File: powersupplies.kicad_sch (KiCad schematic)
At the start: 25 parts, among them U1 OB2222M, U2 STK17-3.3

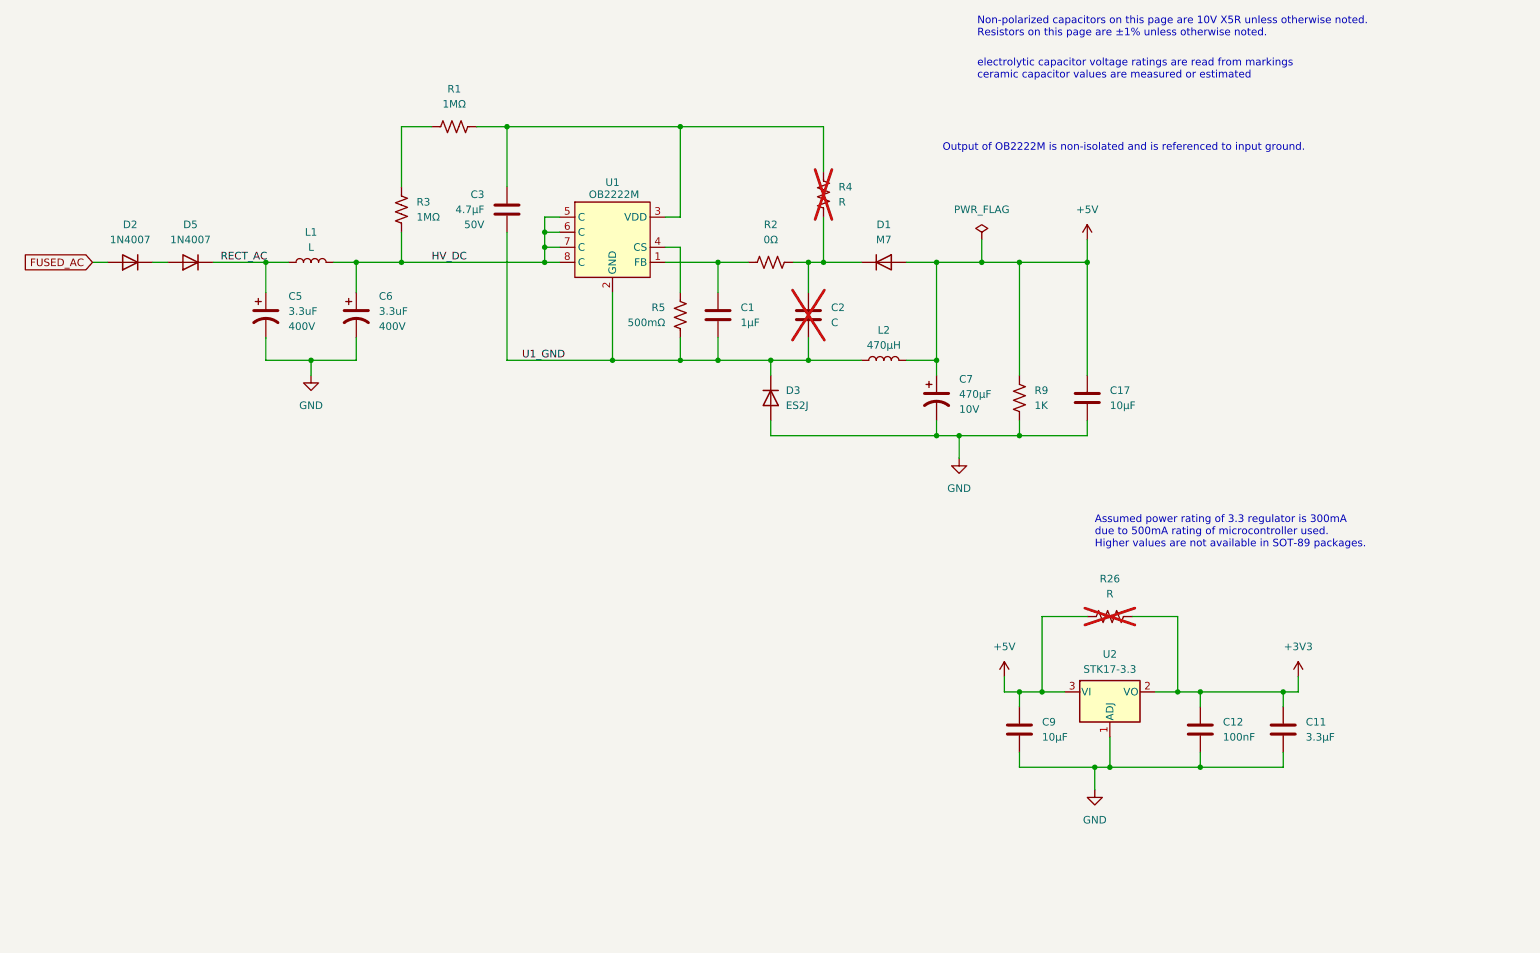
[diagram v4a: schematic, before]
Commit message: All values determined for schematic. From measurements, datasheets, or reading markings.
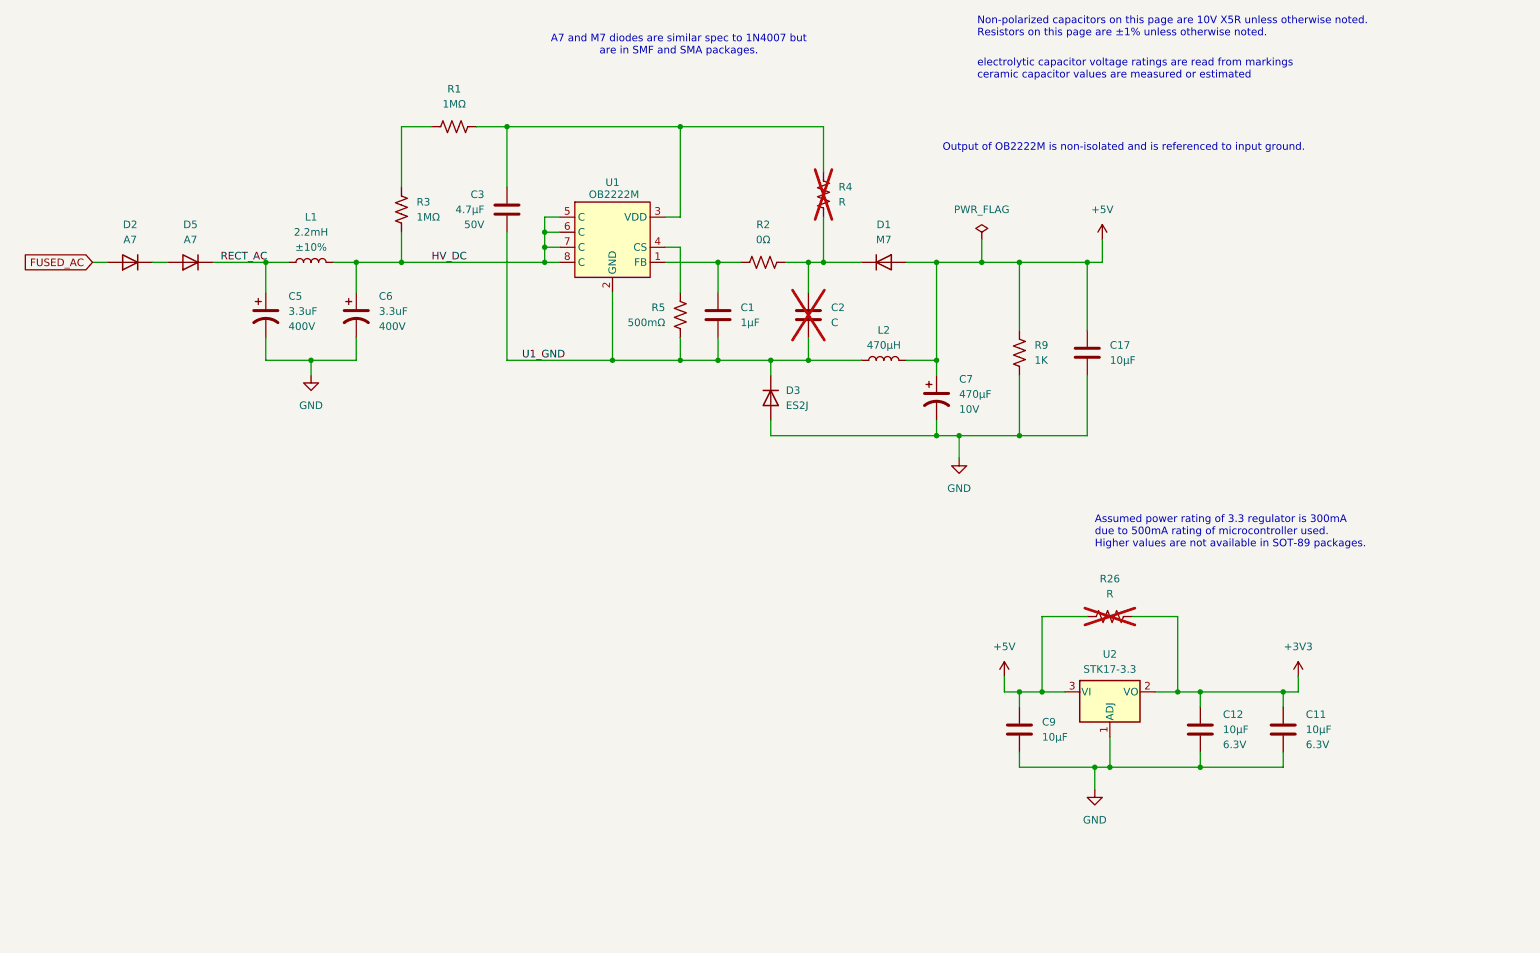
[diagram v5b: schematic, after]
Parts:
- C11: value 3.3µF -> 10µF; Voltage (none) -> 6.3V
- C12: value 100nF -> 10µF; Voltage (none) -> 6.3V
- D2, D5: value 1N4007 -> A7
- L1: value L -> 2.2mH; Tolerance (none) -> ±10%
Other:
- note added: "A7 and M7 diodes are similar spec to 1N4007 but are in SMF and SMA packages."
- moved on the sheet: C17, R2, R9
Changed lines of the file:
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@@
 		)
 	)
+	(text "A7 and M7 diodes are similar spec to 1N4007 but\nare in SMF and SMA packages."
+		(exclude_from_sim no)
+		(at 128.016 33.274 0)
+		(effects
+			(font
+				(size 1.27 1.27)
+			)
+		)
+	)
 	(text "electrolytic capacitor voltage ratings are read from markings\nceramic capacitor values are measured or estimated"
 		(exclude_from_sim no)
@@
 	(wire
 		(pts
+			(xy 199.39 69.85) (xy 196.85 69.85)
+		)
+		(stroke
+			(width 0)
+			(type default)
+		)
+	)
+	(wire
+		(pts
 			(xy 49.53 69.85) (xy 58.42 69.85)
 		)
@@
 	(wire
 		(pts
-			(xy 185.42 99.06) (xy 185.42 96.52)
+			(xy 185.42 99.06) (xy 185.42 88.9)
 		)
 		(stroke
@@
 	(wire
 		(pts
-			(xy 196.85 66.04) (xy 196.85 69.85)
+			(xy 199.39 66.04) (xy 199.39 69.85)
 		)
 		(stroke
@@
 	(wire
 		(pts
-			(xy 134.62 69.85) (xy 139.7 69.85)
+			(xy 134.62 69.85) (xy 138.43 69.85)
 		)
 		(stroke
@@
 	(wire
 		(pts
-			(xy 147.32 69.85) (xy 149.86 69.85)
+			(xy 146.05 69.85) (xy 149.86 69.85)
 		)
 		(stroke
@@
 	(wire
 		(pts
-			(xy 196.85 69.85) (xy 196.85 88.9)
+			(xy 196.85 69.85) (xy 196.85 81.28)
 		)
 		(stroke
@@
 	(wire
 		(pts
-			(xy 196.85 99.06) (xy 196.85 96.52)
+			(xy 196.85 99.06) (xy 196.85 88.9)
 		)
 		(stroke
@@
 	(wire
 		(pts
-			(xy 185.42 69.85) (xy 185.42 88.9)
+			(xy 185.42 69.85) (xy 185.42 81.28)
 		)
 		(stroke
@@
 			)
 		)
-		(property "Value" "1N4007"
+		(property "Value" "A7"
 			(at 35.56 66.04 0)
 			(effects
@@
 	(symbol
 		(lib_id "Device:C")
-		(at 196.85 92.71 0)
+		(at 196.85 85.09 0)
 		(unit 1)
 		(exclude_from_sim no)
@@
 		(fields_autoplaced yes)
 		(property "Reference" "C17"
-			(at 200.66 91.4399 0)
+			(at 200.66 83.8199 0)
 			(effects
 				(font
@@
 		)
 		(property "Value" "10µF"
-			(at 200.66 93.9799 0)
+			(at 200.66 86.3599 0)
 			(effects
 				(font
@@
 		)
 		(property "Footprint" "Capacitor_SMD:C_0603_1608Metric"
-			(at 197.8152 96.52 0)
+			(at 197.8152 88.9 0)
 			(effects
 				(font
@@
 		)
 		(property "Datasheet" "~"
-			(at 196.85 92.71 0)
+			(at 196.85 85.09 0)
 			(effects
 				(font
@@
 		)
 		(property "Description" "Unpolarized capacitor"
-			(at 196.85 92.71 0)
+			(at 196.85 85.09 0)
 			(effects
 				(font
@@
 		(fields_autoplaced yes)
 		(property "Reference" "L1"
-			(at 66.04 64.77 90)
+			(at 66.04 62.23 90)
 			(effects
 				(font
@@
 			)
 		)
-		(property "Value" "L"
-			(at 66.04 67.31 90)
+		(property "Value" "2.2mH"
+			(at 66.04 64.77 90)
 			(effects
 				(font
@@
 			)
 		)
+		(property "Tolerance" "±10%"
+			(at 66.04 67.31 90)
+			(effects
+				(font
+					(size 1.27 1.27)
+				)
+			)
+		)
 		(pin "1"
 		)
@@
 	(symbol
 		(lib_id "Device:R_US")
-		(at 143.51 69.85 90)
+		(at 142.24 69.85 90)
 		(unit 1)
 		(exclude_from_sim no)
@@
 		(fields_autoplaced yes)
 		(property "Reference" "R2"
-			(at 143.51 63.5 90)
+			(at 142.24 63.5 90)
 			(effects
 				(font
@@
 		)
 		(property "Value" "0Ω"
-			(at 143.51 66.04 90)
+			(at 142.24 66.04 90)
 			(effects
 				(font
@@
 		)
 		(property "Footprint" "Resistor_SMD:R_0603_1608Metric"
-			(at 143.764 68.834 90)
+			(at 142.494 68.834 90)
 			(effects
 				(font
@@
 		)
 		(property "Datasheet" "~"
-			(at 143.51 69.85 0)
+			(at 142.24 69.85 0)
 			(effects
 				(font
@@
 		)
 		(property "Description" "Resistor, US symbol"
-			(at 143.51 69.85 0)
+			(at 142.24 69.85 0)
 			(effects
 				(font
@@
 	(symbol
 		(lib_id "Device:R_US")
-		(at 185.42 92.71 0)
+		(at 185.42 85.09 0)
 		(unit 1)
 		(exclude_from_sim no)
@@
 		(fields_autoplaced yes)
 		(property "Reference" "R9"
-			(at 187.96 91.4399 0)
+			(at 187.96 83.8199 0)
 			(effects
 				(font
@@
 		)
 		(property "Value" "1K"
-			(at 187.96 93.9799 0)
+			(at 187.96 86.3599 0)
 			(effects
 				(font
@@
 		)
 		(property "Footprint" "Resistor_SMD:R_0603_1608Metric"
-			(at 186.436 92.964 90)
+			(at 186.436 85.344 90)
 			(effects
 				(font
@@
 		)
 		(property "Datasheet" "~"
-			(at 185.42 92.71 0)
+			(at 185.42 85.09 0)
 			(effects
 				(font
@@
 		)
 		(property "Description" "Resistor, US symbol"
-			(at 185.42 92.71 0)
+			(at 185.42 85.09 0)
 			(effects
 				(font
@@
 	(symbol
 		(lib_id "power:+5V")
-		(at 196.85 66.04 0)
+		(at 199.39 66.04 0)
 		(unit 1)
 		(exclude_from_sim no)
@@
 		(fields_autoplaced yes)
 		(property "Reference" "#PWR022"
-			(at 196.85 69.85 0)
+			(at 199.39 69.85 0)
 			(effects
 				(font
@@
 		)
 		(property "Value" "+5V"
-			(at 196.85 60.96 0)
+			(at 199.39 60.96 0)
 			(effects
 				(font
@@
 		)
 		(property "Footprint" ""
-			(at 196.85 66.04 0)
+			(at 199.39 66.04 0)
 			(effects
 				(font
@@
 		)
 		(property "Datasheet" ""
-			(at 196.85 66.04 0)
+			(at 199.39 66.04 0)
 			(effects
 				(font
@@
 		)
 		(property "Description" "Power symbol creates a global label with name \"+5V\""
-			(at 196.85 66.04 0)
+			(at 199.39 66.04 0)
 			(effects
 				(font
@@
 			)
 		)
-		(property "Value" "1N4007"
+		(property "Value" "A7"
 			(at 45.72 66.04 0)
 			(effects
@@
 		(fields_autoplaced yes)
 		(property "Reference" "C11"
-			(at 233.68 147.3199 0)
+			(at 233.68 146.0499 0)
 			(effects
 				(font
@@
 			)
 		)
-		(property "Value" "3.3µF"
-			(at 233.68 149.8599 0)
+		(property "Value" "10µF"
+			(at 233.68 148.5899 0)
 			(effects
 				(font
@@
 			)
 		)
+		(property "Voltage" "6.3V"
+			(at 233.68 151.1299 0)
+			(effects
+				(font
+					(size 1.27 1.27)
+				)
+				(justify right)
+			)
+		)
 		(pin "1"
 		)
@@
 		(fields_autoplaced yes)
 		(property "Reference" "C12"
-			(at 219.71 147.3199 0)
+			(at 219.71 146.0499 0)
 			(effects
 				(font
@@
 			)
 		)
-		(property "Value" "100nF"
-			(at 219.71 149.8599 0)
+		(property "Value" "10µF"
+			(at 219.71 148.5899 0)
 			(effects
 				(font
@@
 			)
 		)
+		(property "Voltage" "6.3V"
+			(at 219.71 151.1299 0)
+			(effects
+				(font
+					(size 1.27 1.27)
+				)
+				(justify right)
+			)
+		)

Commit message: Fixed plug and receptacle foots. No components left to fix but L1? And the silk and fab layers. And some kind of labeling of the design.
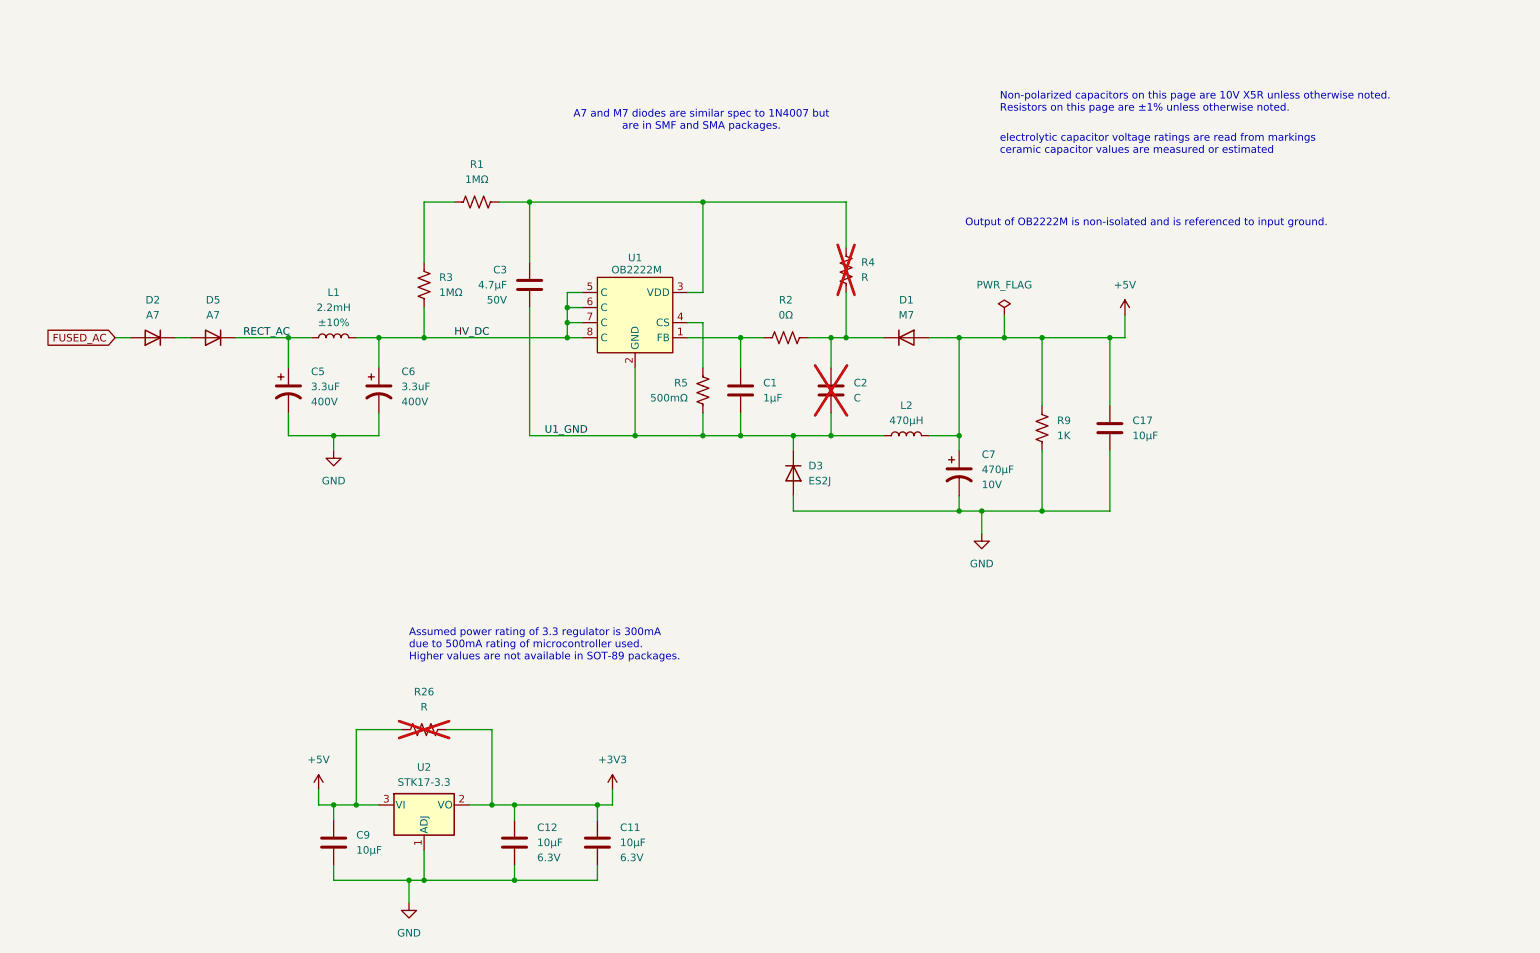
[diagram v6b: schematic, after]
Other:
- moved on the sheet: C1, C11, C12, C17, C2, C3, C5, C6, C7, C9, D1, D2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

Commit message: Renamed things. Removed reference image. Ready for the world.
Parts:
- U1: symbol merossspecific:OB2222M -> designspecific:OB2222M
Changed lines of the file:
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@@
 		)
 		(instances
-			(project "Meross smart outlet reverse"
+			(project "smart-outlet-m-reverse"
 				(path "/0b789f5a-74d1-4f81-bd1f-7ac838c6392e/fc2455a2-d0e8-4734-8077-69cf72fecbb3"
 					(reference "C3")
@@
 		)
 		(instances
-			(project "Meross smart outlet reverse"
+			(project "smart-outlet-m-reverse"
 				(path "/0b789f5a-74d1-4f81-bd1f-7ac838c6392e/fc2455a2-d0e8-4734-8077-69cf72fecbb3"
 					(reference "R1")
@@
 		)
 		(instances
-			(project "Meross smart outlet reverse"
+			(project "smart-outlet-m-reverse"
 				(path "/0b789f5a-74d1-4f81-bd1f-7ac838c6392e/fc2455a2-d0e8-4734-8077-69cf72fecbb3"
 					(reference "D3")
@@
 		)
 		(instances
-			(project "Meross smart outlet reverse"
+			(project "smart-outlet-m-reverse"
 				(path "/0b789f5a-74d1-4f81-bd1f-7ac838c6392e/fc2455a2-d0e8-4734-8077-69cf72fecbb3"
 					(reference "C6")
@@
 		)
 		(instances
-			(project "Meross smart outlet reverse"
+			(project "smart-outlet-m-reverse"
 				(path "/0b789f5a-74d1-4f81-bd1f-7ac838c6392e/fc2455a2-d0e8-4734-8077-69cf72fecbb3"
 					(reference "C17")
@@
 		)
 		(instances
-			(project "Meross smart outlet reverse"
+			(project "smart-outlet-m-reverse"
 				(path "/0b789f5a-74d1-4f81-bd1f-7ac838c6392e/fc2455a2-d0e8-4734-8077-69cf72fecbb3"
 					(reference "C9")
@@
 		)
 		(instances
-			(project "Meross smart outlet reverse"
+			(project "smart-outlet-m-reverse"
 				(path "/0b789f5a-74d1-4f81-bd1f-7ac838c6392e/fc2455a2-d0e8-4734-8077-69cf72fecbb3"
 					(reference "C2")
@@
 		)
 		(instances
-			(project "Meross smart outlet reverse"
+			(project "smart-outlet-m-reverse"
 				(path "/0b789f5a-74d1-4f81-bd1f-7ac838c6392e/fc2455a2-d0e8-4734-8077-69cf72fecbb3"
 					(reference "#PWR023")
@@
 		)
 		(instances
-			(project "Meross smart outlet reverse"
+			(project "smart-outlet-m-reverse"
 				(path "/0b789f5a-74d1-4f81-bd1f-7ac838c6392e/fc2455a2-d0e8-4734-8077-69cf72fecbb3"
 					(reference "C1")
@@
 		)
 		(instances
-			(project "Meross smart outlet reverse"
+			(project "smart-outlet-m-reverse"
 				(path "/0b789f5a-74d1-4f81-bd1f-7ac838c6392e/fc2455a2-d0e8-4734-8077-69cf72fecbb3"
 					(reference "R4")
@@
 		)
 		(instances
-			(project "Meross smart outlet reverse"
+			(project "smart-outlet-m-reverse"
 				(path "/0b789f5a-74d1-4f81-bd1f-7ac838c6392e/fc2455a2-d0e8-4734-8077-69cf72fecbb3"
 					(reference "#PWR022")
@@
 	)
 	(symbol
-		(lib_id "merossspecific:OB2222M")
+		(lib_id "designspecific:OB2222M")
 		(at 120.65 78.74 0)
 		(unit 1)
@@
 		)
 		(instances
-			(project "Meross smart outlet reverse"
+			(project "smart-outlet-m-reverse"
 				(path "/0b789f5a-74d1-4f81-bd1f-7ac838c6392e/fc2455a2-d0e8-4734-8077-69cf72fecbb3"
 					(reference "C11")
@@
 		)
 		(instances
-			(project "Meross smart outlet reverse"
+			(project "smart-outlet-m-reverse"
 				(path "/0b789f5a-74d1-4f81-bd1f-7ac838c6392e/fc2455a2-d0e8-4734-8077-69cf72fecbb3"
 					(reference "#PWR09")
@@
 		)
 		(instances
-			(project "Meross smart outlet reverse"
+			(project "smart-outlet-m-reverse"
 				(path "/0b789f5a-74d1-4f81-bd1f-7ac838c6392e/fc2455a2-d0e8-4734-8077-69cf72fecbb3"
 					(reference "C12")
